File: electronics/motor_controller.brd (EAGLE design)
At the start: 100 x 100 mm, 45 parts

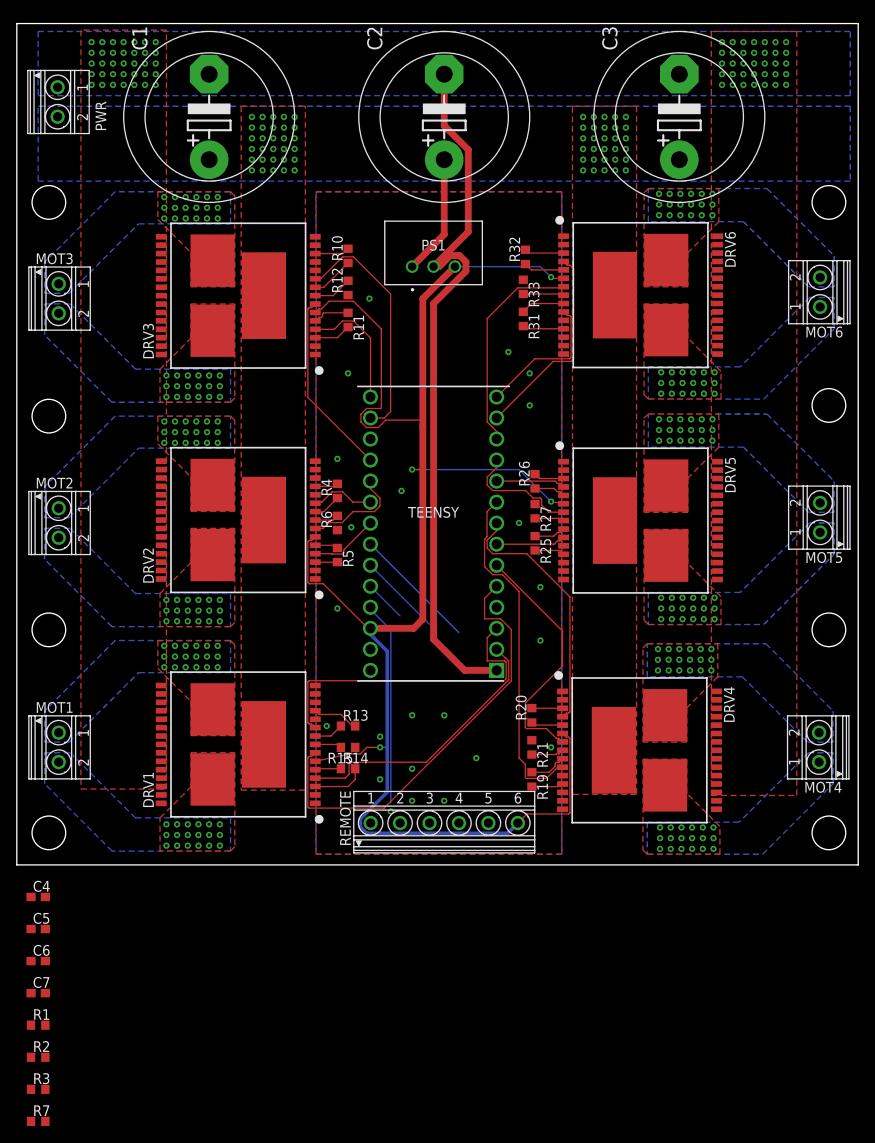
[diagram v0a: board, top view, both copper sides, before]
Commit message: Design Review V1
Changed the signal levels from V+ to 3V3 with 3K3 resistors
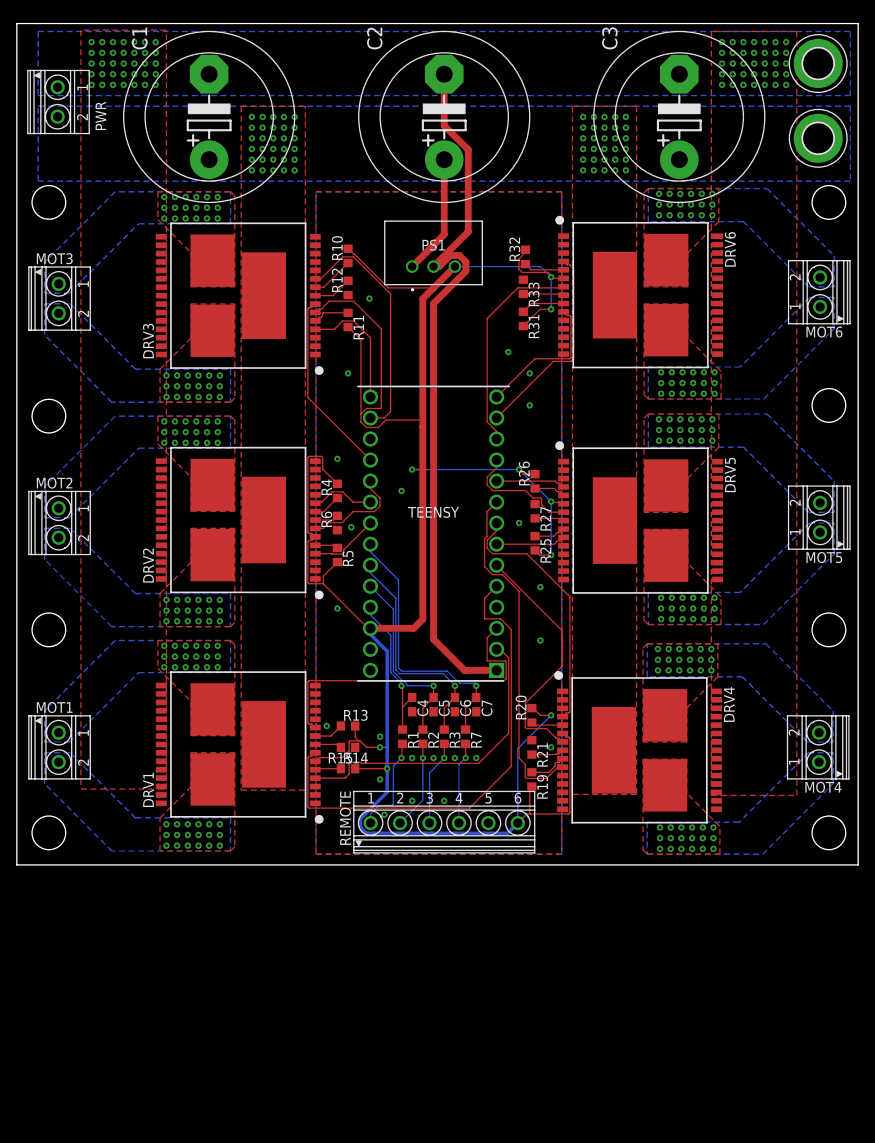
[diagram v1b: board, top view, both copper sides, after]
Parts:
- added H1, H2: MOUNT-PAD-ROUND3.6, holes:3,6-PAD
- moved R7 68.3 mm to (53.3, 15.2), turned to 270 degrees
- moved R3 63.9 mm to (50.8, 15.2), turned to 270 degrees
- moved C7 62.3 mm to (54.6, 19.1), turned to 270 degrees
- moved R2 59.5 mm to (48.3, 15.2), turned to 270 degrees
- moved C6 58.2 mm to (52.1, 19.1), turned to 270 degrees
- moved R1 55.2 mm to (45.8, 15.2), turned to 270 degrees
- moved C5 54.0 mm to (49.5, 19.1), turned to 270 degrees
- moved C4 50.0 mm to (47.0, 19.1), turned to 270 degrees
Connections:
- net +3V3: now also R10.2, R11.2, R13.2, R14.2, R19.2, R20.2, R25.2, R26.2, R31.2, R32.2, R4.2, R5.2
- net GND: now also H2.B3,6
- net V+: now also H1.B3,6; no longer R10.2, R11.2, R13.2, R14.2, R19.2, R20.2, R25.2, R26.2, R31.2, R32.2, R4.2, R5.2
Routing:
- net +3V3: track 203.0 -> 298.2 mm, vias 4 -> 9
- net V+: track 64.3 -> 14.3 mm
- net N$2: track 4.98 -> 22.5 mm, vias 0 -> 1
- net N$3: track 9.93 -> 27.3 mm, vias 0 -> 1
- net N$4: track 14.9 -> 32.1 mm, vias 0 -> 1
- net N$5: track 0.00 -> 11.8 mm, vias 0 -> 1
- net N$11: track 0.00 -> 10.5 mm, vias 0 -> 1
- net N$12: track 0.00 -> 10.1 mm, vias 0 -> 1
- net N$13: track 0.00 -> 9.74 mm, vias 0 -> 1
- net N$1: track 24.2 -> 17.7 mm, vias 0 -> 1
- net PWM_1: track 51.7 -> 57.7 mm
- net INA_1: track 32.8 -> 36.9 mm

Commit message: Added digikey to BOM
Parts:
- C4, C5, C6, C7: value (none) -> 10uF
- R1, R2, R3, R7: value (none) -> 10k
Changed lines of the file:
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@@
 <drawing>
 <settings>
-<setting alwaysvectorfont="yes"/>
+<setting alwaysvectorfont="no"/>
 <setting verticaltext="up"/>
 </settings>
@@
 <attribute name="RS_PRICE-STOCK" value="http://uk.rs-online.com/web/p/products/1245510" x="49.53" y="39.37" size="1.778" layer="27" rot="R180" display="off"/>
 </element>
-<element name="C4" library="rcl" library_urn="urn:adsk.eagle:library:334" package="C0603" package3d_urn="urn:adsk.eagle:package:23616/2" value="" x="46.99" y="19.05" smashed="yes" rot="R270">
+<element name="C4" library="rcl" library_urn="urn:adsk.eagle:library:334" package="C0603" package3d_urn="urn:adsk.eagle:package:23616/2" value="10uF" x="46.99" y="19.05" smashed="yes" rot="R270">
 <attribute name="NAME" x="47.625" y="19.685" size="1.27" layer="25" rot="R270"/>
 <attribute name="SPICEPREFIX" value="C" x="46.99" y="19.05" size="1.778" layer="27" rot="R270" display="off"/>
 <attribute name="VALUE" x="45.085" y="19.685" size="1.27" layer="27" rot="R270"/>
 </element>
-<element name="C5" library="rcl" library_urn="urn:adsk.eagle:library:334" package="C0603" package3d_urn="urn:adsk.eagle:package:23616/2" value="" x="49.53" y="19.05" smashed="yes" rot="R270">
+<element name="C5" library="rcl" library_urn="urn:adsk.eagle:library:334" package="C0603" package3d_urn="urn:adsk.eagle:package:23616/2" value="10uF" x="49.53" y="19.05" smashed="yes" rot="R270">
 <attribute name="NAME" x="50.165" y="19.685" size="1.27" layer="25" rot="R270"/>
 <attribute name="SPICEPREFIX" value="C" x="49.53" y="19.05" size="1.778" layer="27" rot="R270" display="off"/>
 <attribute name="VALUE" x="47.625" y="19.685" size="1.27" layer="27" rot="R270"/>
 </element>
-<element name="C6" library="rcl" library_urn="urn:adsk.eagle:library:334" package="C0603" package3d_urn="urn:adsk.eagle:package:23616/2" value="" x="52.07" y="19.05" smashed="yes" rot="R270">
+<element name="C6" library="rcl" library_urn="urn:adsk.eagle:library:334" package="C0603" package3d_urn="urn:adsk.eagle:package:23616/2" value="10uF" x="52.07" y="19.05" smashed="yes" rot="R270">
 <attribute name="NAME" x="52.705" y="19.685" size="1.27" layer="25" rot="R270"/>
 <attribute name="SPICEPREFIX" value="C" x="52.07" y="19.05" size="1.778" layer="27" rot="R270" display="off"/>
 <attribute name="VALUE" x="50.165" y="19.685" size="1.27" layer="27" rot="R270"/>
 </element>
-<element name="C7" library="rcl" library_urn="urn:adsk.eagle:library:334" package="C0603" package3d_urn="urn:adsk.eagle:package:23616/2" value="" x="54.61" y="19.05" smashed="yes" rot="R270">
+<element name="C7" library="rcl" library_urn="urn:adsk.eagle:library:334" package="C0603" package3d_urn="urn:adsk.eagle:package:23616/2" value="10uF" x="54.61" y="19.05" smashed="yes" rot="R270">
 <attribute name="NAME" x="55.245" y="19.685" size="1.27" layer="25" rot="R270"/>
 <attribute name="SPICEPREFIX" value="C" x="54.61" y="19.05" size="1.778" layer="27" rot="R270" display="off"/>
 <attribute name="VALUE" x="52.705" y="19.685" size="1.27" layer="27" rot="R270"/>
 </element>
-<element name="R1" library="rcl" library_urn="urn:adsk.eagle:library:334" package="R0603" package3d_urn="urn:adsk.eagle:package:23555/2" value="" x="45.847" y="15.24" smashed="yes" rot="R270">
+<element name="R1" library="rcl" library_urn="urn:adsk.eagle:library:334" package="R0603" package3d_urn="urn:adsk.eagle:package:23555/2" value="10k" x="45.847" y="15.24" smashed="yes" rot="R270">
 <attribute name="NAME" x="46.482" y="15.875" size="1.27" layer="25" rot="R270"/>
 <attribute name="SPICEPREFIX" value="R" x="45.847" y="15.24" size="1.778" layer="27" rot="R270" display="off"/>
 <attribute name="VALUE" x="43.942" y="15.875" size="1.27" layer="27" rot="R270"/>
 </element>
-<element name="R2" library="rcl" library_urn="urn:adsk.eagle:library:334" package="R0603" package3d_urn="urn:adsk.eagle:package:23555/2" value="" x="48.26" y="15.24" smashed="yes" rot="R270">
+<element name="R2" library="rcl" library_urn="urn:adsk.eagle:library:334" package="R0603" package3d_urn="urn:adsk.eagle:package:23555/2" value="10k" x="48.26" y="15.24" smashed="yes" rot="R270">
 <attribute name="NAME" x="48.895" y="15.875" size="1.27" layer="25" rot="R270"/>
 <attribute name="SPICEPREFIX" value="R" x="48.26" y="15.24" size="1.778" layer="27" rot="R270" display="off"/>
 <attribute name="VALUE" x="46.355" y="15.875" size="1.27" layer="27" rot="R270"/>
 </element>
-<element name="R3" library="rcl" library_urn="urn:adsk.eagle:library:334" package="R0603" package3d_urn="urn:adsk.eagle:package:23555/2" value="" x="50.8" y="15.24" smashed="yes" rot="R270">
+<element name="R3" library="rcl" library_urn="urn:adsk.eagle:library:334" package="R0603" package3d_urn="urn:adsk.eagle:package:23555/2" value="10k" x="50.8" y="15.24" smashed="yes" rot="R270">
 <attribute name="NAME" x="51.435" y="15.875" size="1.27" layer="25" rot="R270"/>
 <attribute name="SPICEPREFIX" value="R" x="50.8" y="15.24" size="1.778" layer="27" rot="R270" display="off"/>
 <attribute name="VALUE" x="48.895" y="15.875" size="1.27" layer="27" rot="R270"/>
 </element>
-<element name="R7" library="rcl" library_urn="urn:adsk.eagle:library:334" package="R0603" package3d_urn="urn:adsk.eagle:package:23555/2" value="" x="53.34" y="15.24" smashed="yes" rot="R270">
+<element name="R7" library="rcl" library_urn="urn:adsk.eagle:library:334" package="R0603" package3d_urn="urn:adsk.eagle:package:23555/2" value="10k" x="53.34" y="15.24" smashed="yes" rot="R270">
 <attribute name="NAME" x="53.975" y="15.875" size="1.27" layer="25" rot="R270"/>
 <attribute name="SPICEPREFIX" value="R" x="53.34" y="15.24" size="1.778" layer="27" rot="R270" display="off"/>
